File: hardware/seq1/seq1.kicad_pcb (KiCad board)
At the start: 2 copper layers, 174 x 100 mm, 111 parts, among them J1 AudioJack2_SwitchT, J2 AudioJack2_SwitchT, J3 Conn_02x08_Odd_Even, J4 AudioJack2_SwitchT, J5 AudioJack2_SwitchT, J7 Conn_01x02, J8 AudioJack2_SwitchT, J9 AudioJack2_SwitchT, Q1 2N3904, SW9 PEC12R-3220F-S0024, U10 TL072, U11 Neopixel Keypad 1x4, U12 Neopixel Keypad 1x4, U13 Neopixel Keypad 1x4, U14 Neopixel Keypad 1x4, U15 1x2 LED Keypad, U2 74HC4051, U3 74HC4051, U5 128x64 0.96" OLED I2C, U6 TL074, U7 TLV1117-33, U8 74HC4051, U9 74HC4051

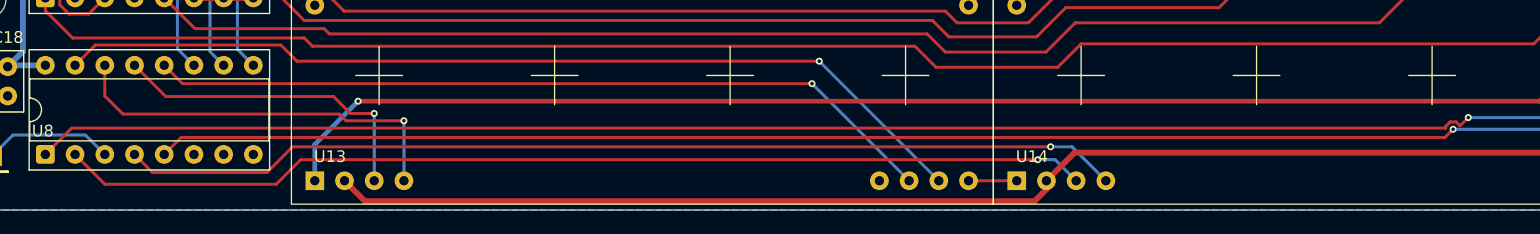
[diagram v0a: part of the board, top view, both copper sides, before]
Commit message: Some schematic cleanup
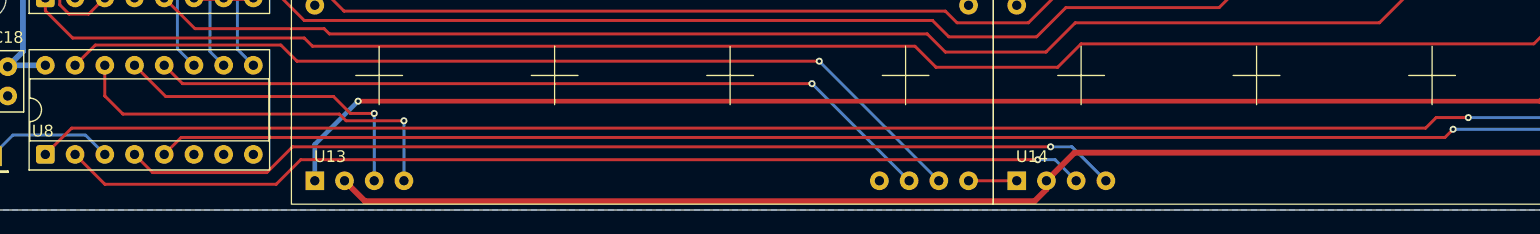
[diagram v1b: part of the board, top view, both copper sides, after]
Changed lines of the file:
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@@
+	)
+	(segment
+		(start 190.6 127.1)
+		(end 187.85 127.1)
+		(width 0.254)
+		(layer "F.Cu")
+		(net 91)
 	)
 	(segment
@@
 	)
 	(segment
-		(start 188.672 127.839873)
-		(end 188.672 128)
-		(width 0.254)
-		(layer "F.Cu")
-		(net 91)
-	)
-	(segment
-		(start 188.672 128)
+		(start 186.95 128)
 		(end 71.22 128)
 		(width 0.254)
@@
 	)
 	(segment
-		(start 189.560127 127.472)
-		(end 189.039873 127.472)
+		(start 187.85 127.1)
+		(end 186.95 128)
 		(width 0.254)
 		(layer "F.Cu")
-		(net 91)
-	)
-	(segment
-		(start 189.039873 127.472)
-		(end 188.672 127.839873)
-		(width 0.254)
-		(layer "F.Cu")
-		(net 91)
-	)
-	(segment
-		(start 189.894063 127.805937)
-		(end 189.560127 127.472)
-		(width 0.254)
-		(layer "F.Cu")
-		(net 91)
-	)
-	(segment
-		(start 190.6 127.1)
-		(end 189.894063 127.805937)
-		(width 0.254)
-		(layer "F.Cu")
